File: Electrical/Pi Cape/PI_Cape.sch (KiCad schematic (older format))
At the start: 8 parts

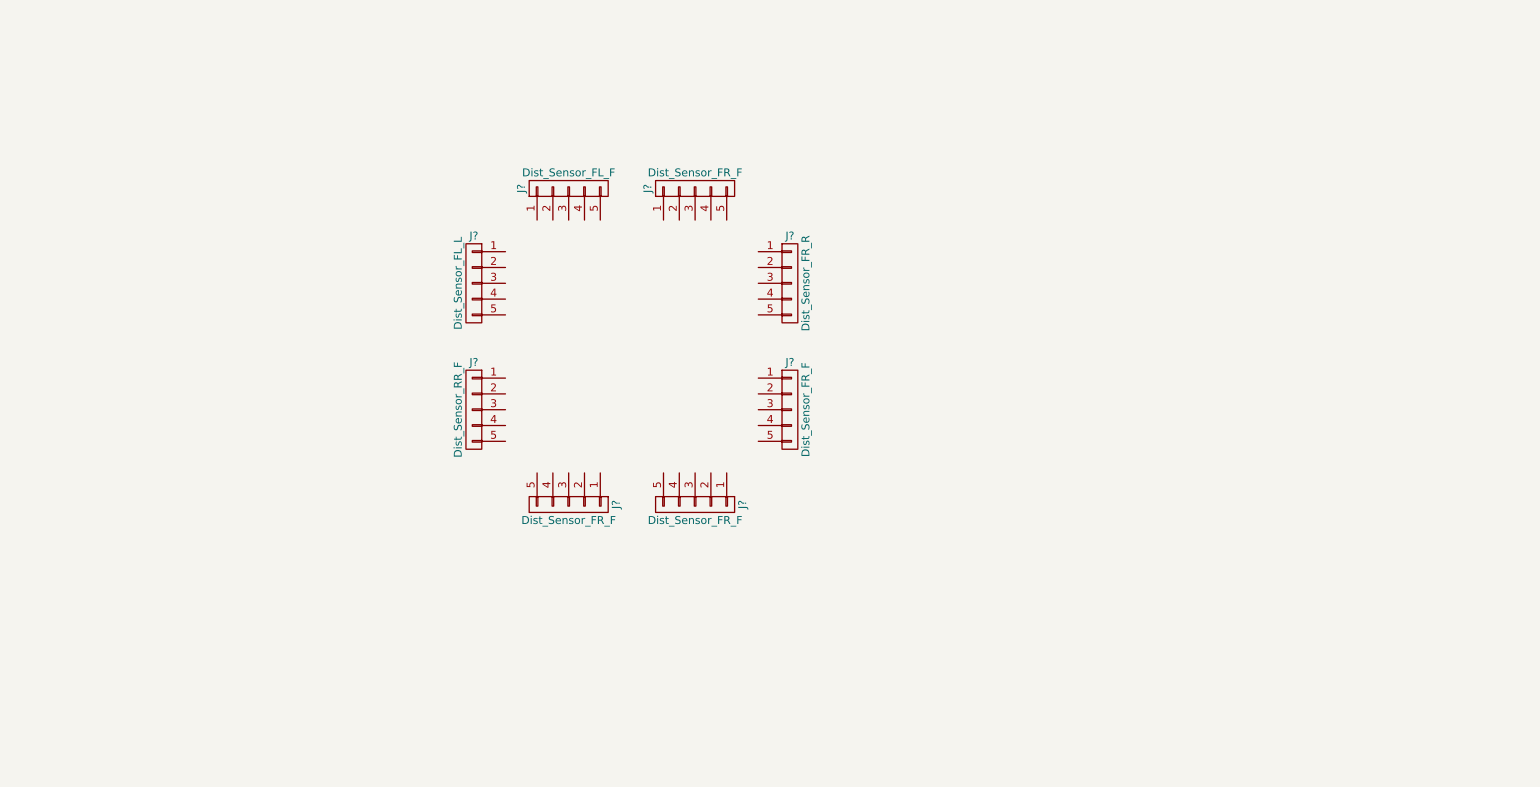
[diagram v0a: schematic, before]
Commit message: updated Pi and Arduino external connection. Finished base Pi schematic
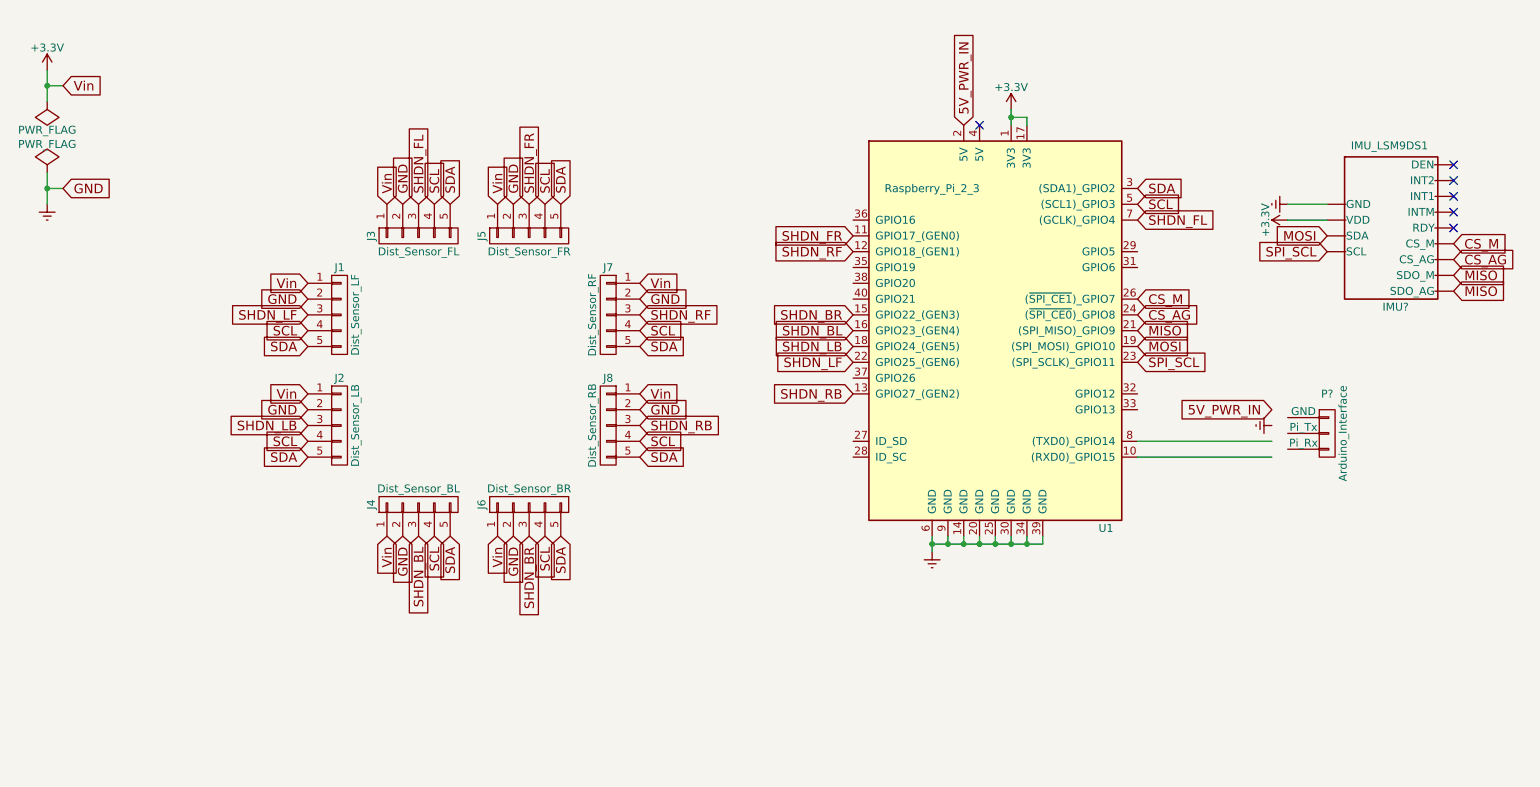
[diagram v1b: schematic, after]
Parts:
- added IMU?: IMU_LSM9DS1, symbol IMU_LSM9DS1
- added P?: Arduino_Interface, symbol Arduino_Interface
- added U1: Raspberry_Pi_2_3, Pin_Headers:Pin_Header_Straight_2x20, symbol Raspberry_Pi_2_3
- J1: renamed from J?; value Dist_Sensor_FL_L -> Dist_Sensor_LF
- J2: renamed from J?; value Dist_Sensor_RR_F -> Dist_Sensor_LB
- J3: renamed from J?; value Dist_Sensor_FL_F -> Dist_Sensor_FL
- J4: renamed from J?; value Dist_Sensor_FR_F -> Dist_Sensor_BL
- J5: renamed from J?; value Dist_Sensor_FR_F -> Dist_Sensor_FR
- J6: renamed from J?; value Dist_Sensor_FR_F -> Dist_Sensor_BR
- J7: renamed from J?; value Dist_Sensor_FR_R -> Dist_Sensor_RF
- J8: renamed from J?; value Dist_Sensor_FR_F -> Dist_Sensor_RB
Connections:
- net labels added: +3.3V, 5V_PWR_IN, CS_AG, CS_M, Earth, GND, MISO, MOSI, SCL, SDA, SHDN_BL, SHDN_BR, SHDN_FL, SHDN_FR, SHDN_LB, SHDN_LF, SHDN_RB, SHDN_RF, SPI_SCL, Vin
- wire segments 0 -> 20
- no-connect marks 0 -> 6
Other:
- moved on the sheet: J1, J2, J3, J4, J5, J6, J7, J8

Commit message: finished updates on pi schematic, working on footprints next
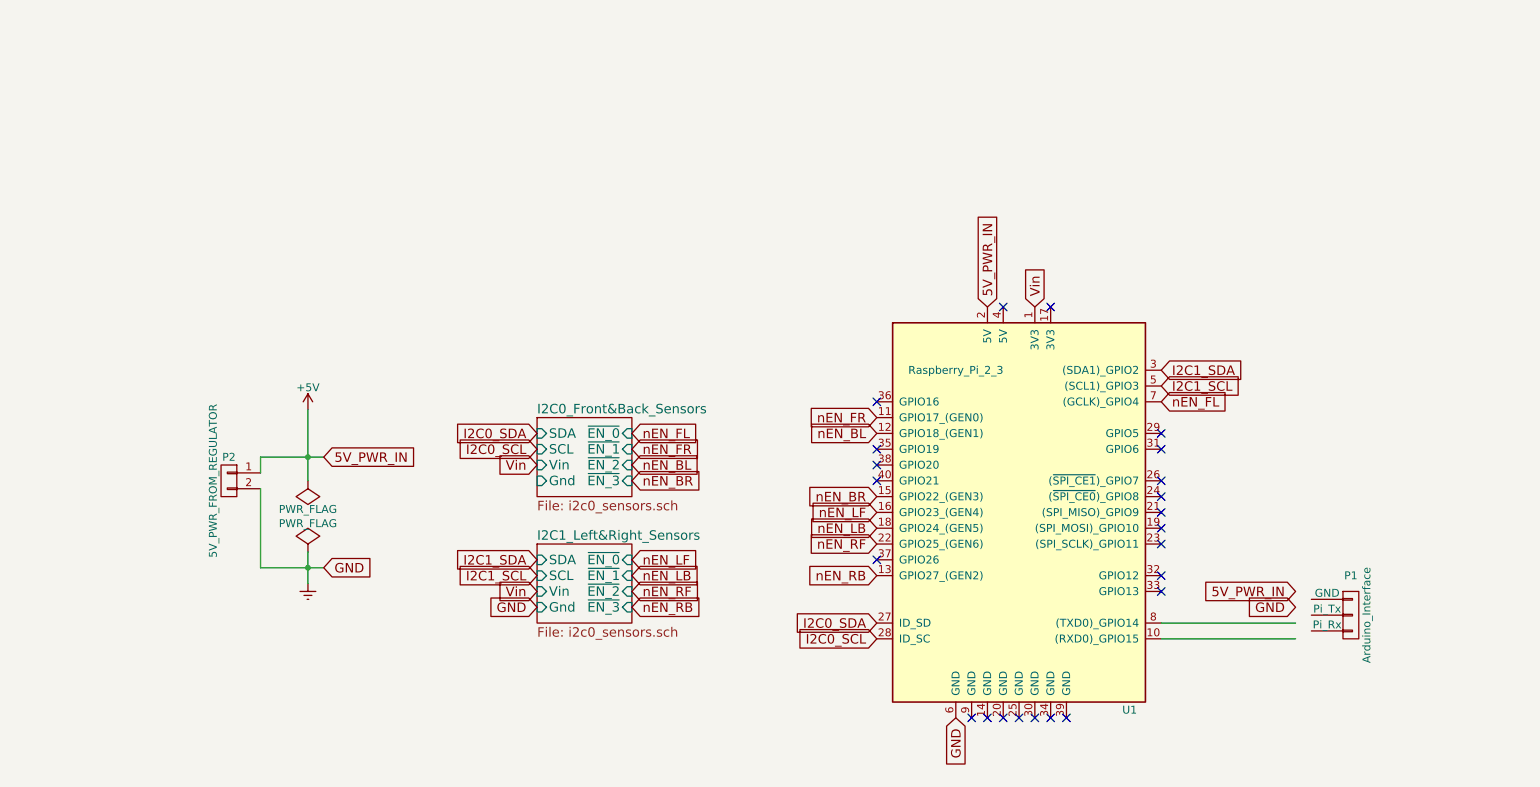
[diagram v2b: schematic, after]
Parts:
- removed IMU?: IMU_LSM9DS1, symbol IMU_LSM9DS1
- removed J1: Dist_Sensor_LF, symbol CONN_01X05
- removed J2: Dist_Sensor_LB, symbol CONN_01X05
- removed J3: Dist_Sensor_FL, symbol CONN_01X05
- removed J4: Dist_Sensor_BL, symbol CONN_01X05
- removed J5: Dist_Sensor_FR, symbol CONN_01X05
- removed J6: Dist_Sensor_BR, symbol CONN_01X05
- removed J7: Dist_Sensor_RF, symbol CONN_01X05
- removed J8: Dist_Sensor_RB, symbol CONN_01X05
- added P2: 5V_PWR_FROM_REGULATOR, symbol CONN_01X02
- gave numbers to parts that had none: 1
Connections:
- net labels added: +5V, I2C0_SCL, I2C0_SDA, I2C1_SCL, I2C1_SDA, nEN_BL, nEN_BR, nEN_FL, nEN_FR, nEN_LB, nEN_LF, nEN_RB, nEN_RF
- net labels removed: +3.3V, CS_AG, CS_M, MISO, MOSI, SCL, SDA, SHDN_BL, SHDN_BR, SHDN_FL, SHDN_FR, SHDN_LB, SHDN_LF, SHDN_RB, SHDN_RF, SPI_SCL
- wire segments 20 -> 8
- no-connect marks 6 -> 23
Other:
- moved on the sheet: P1, U1

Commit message: finished footprints on Pi cape. onto layouts
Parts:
- P1: footprint (none) -> Pi Cape Footprints:Pin_Header_Latched_1x03
- P2: footprint (none) -> Pi Cape Footprints:Pin_Header_Latched_1x02
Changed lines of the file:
@@
 	1    0    0    -1
 $EndComp
-Wire Wire Line
-	7900 4250 8750 4250
-Wire Wire Line
-	7900 4350 8750 4350
 Text GLabel 7100 2250 1    60   Input ~ 0
 Vin
@@
 	2500 2900 2500 3350
 NoConn ~ 6900 2250
-$Comp
-L Arduino_Interface P1
-U 1 1 5A9921FD
-P 9100 4200
-F 0 "P1" H 9100 4450 50  0000 C CNN
-F 1 "Arduino_Interface" V 9200 4200 50  0000 C CNN
-F 2 "" H 9100 4200 50  0000 C CNN
-F 3 "" H 9100 4200 50  0000 C CNN
-	1    9100 4200
-	1    0    0    -1
-$EndComp
-Text GLabel 8750 4050 0    60   Input ~ 0
-5V_PWR_IN
 Text GLabel 6800 2250 1    60   Input ~ 0
 5V_PWR_IN
@@
 NoConn ~ 7900 3150
 NoConn ~ 7900 3950
-NoConn ~ 7900 4050
 NoConn ~ 7200 2250
 NoConn ~ 6700 4850
@@
 F 0 "P2" H 2000 3500 50  0000 C CNN
 F 1 "5V_PWR_FROM_REGULATOR" V 2100 3350 50  0000 C CNN
-F 2 "" H 2000 3350 50  0000 C CNN
+F 2 "Pi Cape Footprints:Pin_Header_Latched_1x02" H 2000 3350 50  0001 C CNN
 F 3 "" H 2000 3350 50  0000 C CNN
 	1    2000 3350
@@
 Text GLabel 3950 4150 0    60   Input ~ 0
 GND
-Text GLabel 8750 4150 0    60   Input ~ 0
+Text GLabel 3950 3350 0    60   Input ~ 0
 GND
+NoConn ~ 7900 4050
+Wire Wire Line
+	8300 4250 7900 4250
+Wire Wire Line
+	7900 4350 8300 4350
+Text GLabel 8300 4150 0    60   Input ~ 0
+GND
+$Comp
+L Arduino_Interface P1
+U 1 1 5AB07671
+P 8550 4250
+F 0 "P1" H 8550 4450 50  0000 C CNN
+F 1 "Arduino_Interface" V 8650 4250 50  0000 C CNN
+F 2 "Pi Cape Footprints:Pin_Header_Latched_1x03" H 8550 4250 50  0001 C CNN
+F 3 "" H 8550 4250 50  0000 C CNN
+	1    8550 4250
+	1    0    0    -1
+$EndComp
 $EndSCHEMATC

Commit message: updated pi cape to have 7-seg and spaced components in layout
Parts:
- added U2: 7-segment_LED, Pin_Headers:Pin_Header_Straight_1x05, symbol 7-segment_LED
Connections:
- net +5V: now also U2.3 (5V)
- net Earth: now also U2.4 (GND)
- net I2C1_SCL: now also U2.2 (SCL)
- net I2C1_SDA: now also U2.1 (SDA)
- net Vin: now also U2.5 (3.3V)
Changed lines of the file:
@@
 	1    0    0    -1
 $EndComp
+$Comp
+L 7-segment_LED U2
+U 1 1 5AB1C163
+P 9250 3400
+F 0 "U2" H 9250 2650 60  0000 C CNN
+F 1 "7-segment_LED" H 9250 2800 60  0000 C CNN
+F 2 "Pin_Headers:Pin_Header_Straight_1x05" H 9150 3200 60  0001 C CNN
+F 3 "" H 9150 3200 60  0000 C CNN
+	1    9250 3400
+	0    -1   -1   0
+$EndComp
+Text GLabel 9300 3200 0    60   Input ~ 0
+GND
+Text GLabel 9300 3350 0    60   Input ~ 0
+5V_PWR_IN
+Text GLabel 9300 3050 0    60   Input ~ 0
+Vin
+Text GLabel 9300 3650 0    60   Input ~ 0
+I2C1_SDA
+Text GLabel 9300 3500 0    60   Input ~ 0
+I2C1_SCL
 $EndSCHEMATC
